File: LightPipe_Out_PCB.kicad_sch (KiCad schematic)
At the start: 9 parts, among them J1 Conn_01x03, J2 Conn_01x02, J3 Conn_01x04, J4 Conn_01x04, J5 Conn_01x04, J6 Conn_01x01, J7 Conn_01x01, J8 Conn_01x02, J9 Conn_01x03

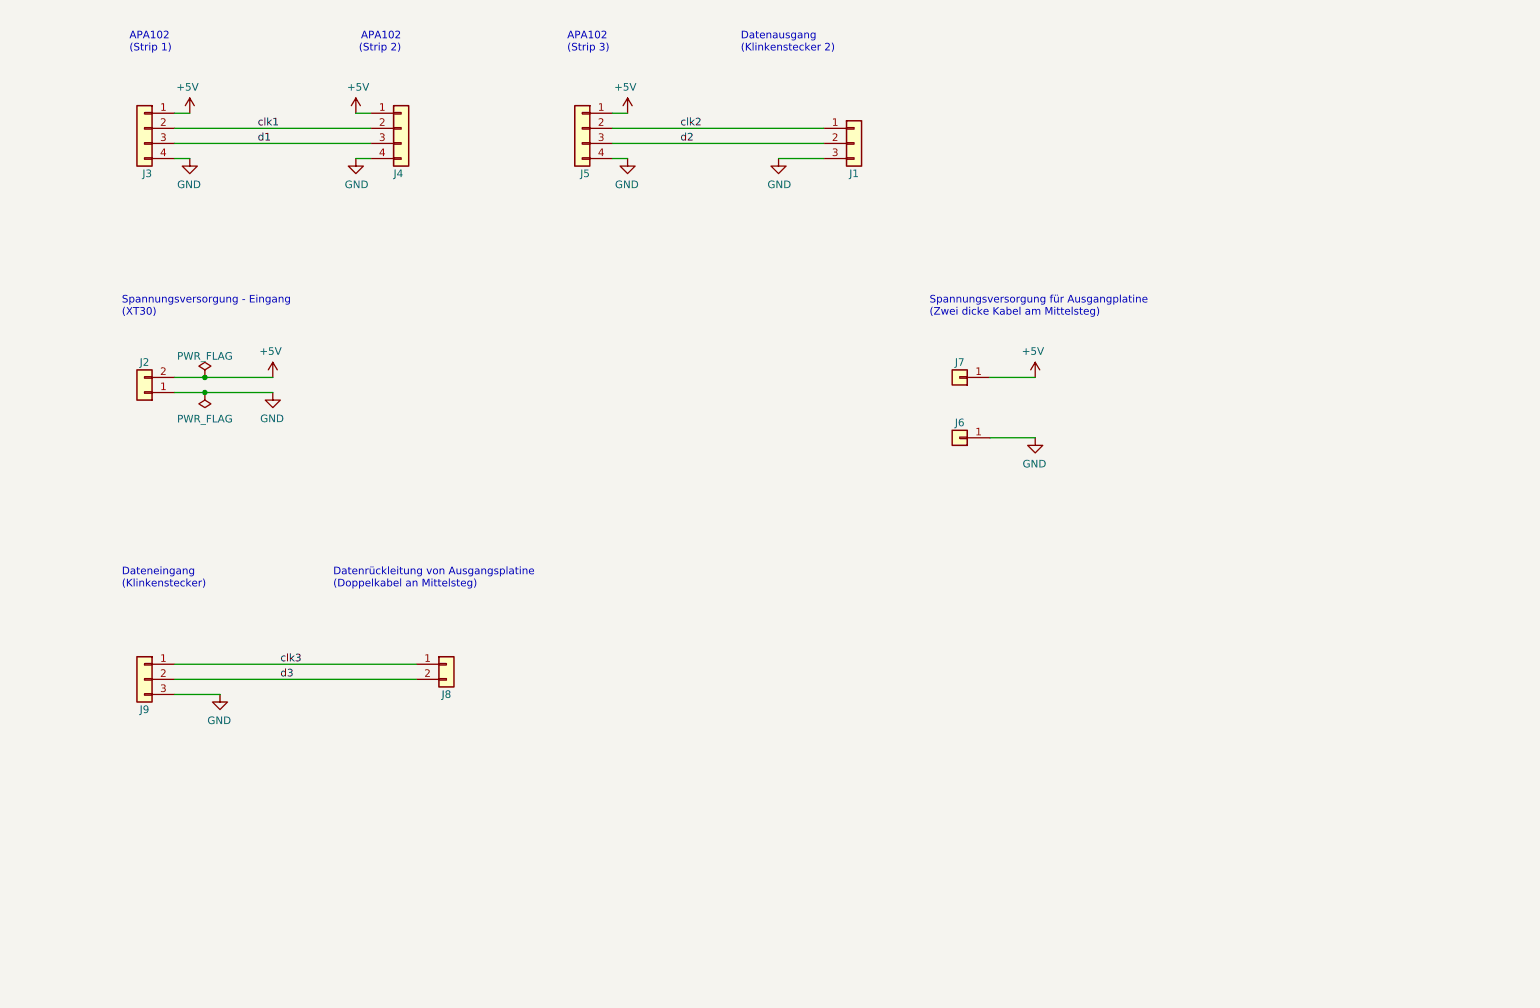
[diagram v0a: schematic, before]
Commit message: [PCB] New Design features to use the PCB as In- and Out-PCB
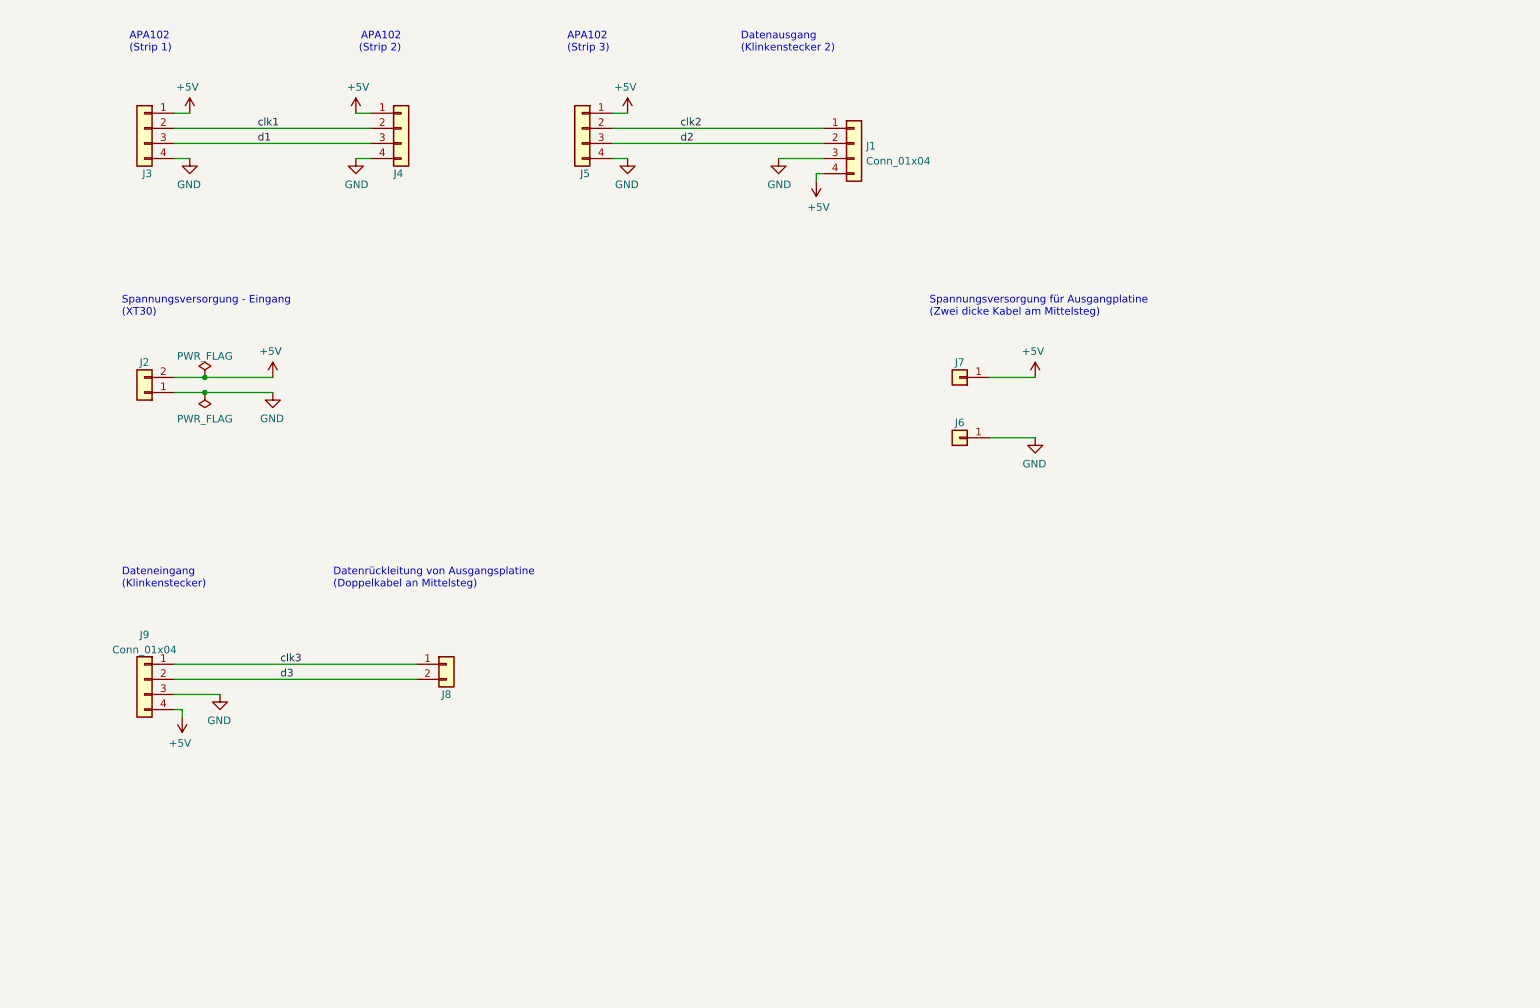
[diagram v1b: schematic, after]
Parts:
- removed J1, J9: Conn_01x03, h8-Connectors:Lumberg-KLB-4-Klinkensteckverbinder-3_5, symbol Connector_Generic:Conn_01x03
- added J1, J9: Conn_01x04, h8-Connectors:Lumberg-KLB-4-Klinkensteckverbinder-3_5-180deg-turnable, symbol Connector_Generic:Conn_01x04
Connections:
- net +5V: now also J1.4 (Pin_4), J9.4 (Pin_4)
- net GND: now also J1.3 (Pin_3), J9.3 (Pin_3)
- net clk2: now also J1.1 (Pin_1)
- net clk3: now also J9.1 (Pin_1)
- net d2: now also J1.2 (Pin_2)
- net d3: now also J9.2 (Pin_2)
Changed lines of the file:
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@@
+    (stroke (width 0) (type default) (color 0 0 0 0))
+  )
+  (wire (pts (xy 48.26 144.78) (xy 48.26 143.51))
     (stroke (width 0) (type default) (color 0 0 0 0))
   )
@@
     (stroke (width 0) (type default) (color 0 0 0 0))
   )
+  (wire (pts (xy 154.94 54.61) (xy 154.94 53.34))
+    (stroke (width 0) (type default) (color 0 0 0 0))
+  )
   (wire (pts (xy 46.99 87.63) (xy 52.07 87.63))
     (stroke (width 0) (type default) (color 0 0 0 0))
@@
     (stroke (width 0) (type default) (color 0 0 0 0))
   )
+  (wire (pts (xy 154.94 53.34) (xy 156.21 53.34))
+    (stroke (width 0) (type default) (color 0 0 0 0))
+  )
   (wire (pts (xy 46.99 48.26) (xy 80.01 48.26))
     (stroke (width 0) (type default) (color 0 0 0 0))
@@
   )
   (wire (pts (xy 80.01 50.8) (xy 77.47 50.8))
+    (stroke (width 0) (type default) (color 0 0 0 0))
+  )
+  (wire (pts (xy 48.26 143.51) (xy 46.99 143.51))
     (stroke (width 0) (type default) (color 0 0 0 0))
   )
@@
     )
     (pin "1")
-  )
-  (symbol (lib_id "Connector_Generic:Conn_01x03") (at 161.29 48.26 0) (unit 1)
-    (in_bom yes) (on_board yes)
-    (property "Reference" "J1" (id 0) (at 161.29 53.34 0))
-    (property "Value" "Conn_01x03" (id 1) (at 159.258 54.2036 0)
-      (effects (font (size 1.27 1.27)) hide)
-    )
-    (property "Footprint" "h8-Connectors:Lumberg-KLB-4-Klinkensteckverbinder-3_5" (id 2) (at 161.29 48.26 0)
-      (effects (font (size 1.27 1.27)) hide)
-    )
-    (property "Datasheet" "~" (id 3) (at 161.29 48.26 0)
-      (effects (font (size 1.27 1.27)) hide)
-    )
-    (pin "1")
-    (pin "2")
-    (pin "3")
-  )
-  (symbol (lib_id "Connector_Generic:Conn_01x03") (at 41.91 138.43 0) (mirror y) (unit 1)
-    (in_bom yes) (on_board yes)
-    (property "Reference" "J9" (id 0) (at 41.91 143.51 0))
-    (property "Value" "Conn_01x03" (id 1) (at 43.942 144.3736 0)
-      (effects (font (size 1.27 1.27)) hide)
-    )
-    (property "Footprint" "h8-Connectors:Lumberg-KLB-4-Klinkensteckverbinder-3_5" (id 2) (at 41.91 138.43 0)
-      (effects (font (size 1.27 1.27)) hide)
-    )
-    (property "Datasheet" "~" (id 3) (at 41.91 138.43 0)
-      (effects (font (size 1.27 1.27)) hide)
-    )
-    (pin "1")
-    (pin "2")
-    (pin "3")
   )
   (symbol (lib_id "Connector_Generic:Conn_01x02") (at 41.91 90.17 180) (unit 1)
@@
     (pin "1")
   )
+  (symbol (lib_id "power:+5V") (at 48.26 144.78 180) (unit 1)
+    (in_bom yes) (on_board yes)
+    (property "Reference" "#PWR0109" (id 0) (at 48.26 140.97 0)
+      (effects (font (size 1.27 1.27)) hide)
+    )
+    (property "Value" "+5V" (id 1) (at 47.879 149.1742 0))
+    (property "Footprint" "" (id 2) (at 48.26 144.78 0)
+      (effects (font (size 1.27 1.27)) hide)
+    )
+    (property "Datasheet" "" (id 3) (at 48.26 144.78 0)
+      (effects (font (size 1.27 1.27)) hide)
+    )
+    (pin "1")
+  )
+  (symbol (lib_id "Connector_Generic:Conn_01x04") (at 161.29 48.26 0) (unit 1)
+    (in_bom yes) (on_board yes) (fields_autoplaced)
+    (property "Reference" "J1" (id 0) (at 163.322 48.6953 0)
+      (effects (font (size 1.27 1.27)) (justify left))
+    )
+    (property "Value" "Conn_01x04" (id 1) (at 163.322 51.2322 0)
+      (effects (font (size 1.27 1.27)) (justify left))
+    )
+    (property "Footprint" "h8-Connectors:Lumberg-KLB-4-Klinkensteckverbinder-3_5-180deg-turnable" (id 2) (at 161.29 48.26 0)
+      (effects (font (size 1.27 1.27)) hide)
+    )
+    (property "Datasheet" "~" (id 3) (at 161.29 48.26 0)
+      (effects (font (size 1.27 1.27)) hide)
+    )
+    (pin "1")
+    (pin "2")
+    (pin "3")
+    (pin "4")
+  )
+  (symbol (lib_id "Connector_Generic:Conn_01x04") (at 41.91 138.43 0) (mirror y) (unit 1)
+    (in_bom yes) (on_board yes) (fields_autoplaced)
+    (property "Reference" "J9" (id 0) (at 41.91 130.9202 0))
+    (property "Value" "Conn_01x04" (id 1) (at 41.91 133.4571 0))
+    (property "Footprint" "h8-Connectors:Lumberg-KLB-4-Klinkensteckverbinder-3_5-180deg-turnable" (id 2) (at 41.91 138.43 0)
+      (effects (font (size 1.27 1.27)) hide)
+    )
+    (property "Datasheet" "~" (id 3) (at 41.91 138.43 0)
+      (effects (font (size 1.27 1.27)) hide)
+    )
+    (pin "1")
+    (pin "2")
+    (pin "3")
+    (pin "4")
+  )
+  (symbol (lib_id "power:+5V") (at 154.94 54.61 0) (mirror x) (unit 1)
+    (in_bom yes) (on_board yes)
+    (property "Reference" "#PWR0110" (id 0) (at 154.94 50.8 0)
+      (effects (font (size 1.27 1.27)) hide)
+    )
+    (property "Value" "+5V" (id 1) (at 155.321 59.0042 0))
+    (property "Footprint" "" (id 2) (at 154.94 54.61 0)
+      (effects (font (size 1.27 1.27)) hide)
+    )
+    (property "Datasheet" "" (id 3) (at 154.94 54.61 0)
+      (effects (font (size 1.27 1.27)) hide)
+    )
+    (pin "1")
+  )
   (symbol (lib_id "power:PWR_FLAG") (at 52.07 87.63 0) (unit 1)
     (in_bom yes) (on_board yes) (fields_autoplaced)
@@
       (reference "#PWR0108") (unit 1) (value "GND") (footprint "")
     )
-    (path "/00000000-0000-0000-0000-00005f9461d7"
-      (reference "J1") (unit 1) (value "Conn_01x03") (footprint "h8-Connectors:Lumberg-KLB-4-Klinkensteckverbinder-3_5")
+    (path "/41571e1e-d333-463a-84fd-29dc2000eb0b"
+      (reference "#PWR0109") (unit 1) (value "+5V") (footprint "")
+    )
+    (path "/7d2c7984-6535-44bc-a86c-9cec98125d73"
+      (reference "#PWR0110") (unit 1) (value "+5V") (footprint "")
+    )
+    (path "/52137419-c203-4dbe-a47e-235ddc4fd115"
+      (reference "J1") (unit 1) (value "Conn_01x04") (footprint "h8-Connectors:Lumberg-KLB-4-Klinkensteckverbinder-3_5-180deg-turnable")
     )
     (path "/00000000-0000-0000-0000-00005f94666b"
@@
       (reference "J8") (unit 1) (value "Conn_01x02") (footprint "Connector_PinHeader_2.00mm:PinHeader_1x02_P2.00mm_Vertical")
     )
-    (path "/00000000-0000-0000-0000-00005f94634e"
-      (reference "J9") (unit 1) (value "Conn_01x03") (footprint "h8-Connectors:Lumberg-KLB-4-Klinkensteckverbinder-3_5")
-    )
-  )
+    (path "/771c4cae-8f80-4832-b07b-977abc522dad"
+      (reference "J9") (unit 1) (value "Conn_01x04") (footprint "h8-Connectors:Lumberg-KLB-4-Klinkensteckverbinder-3_5-180deg-turnable")
+    )
+  )

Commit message: Changed designators from J? to X? and LD? | Improved Footprints
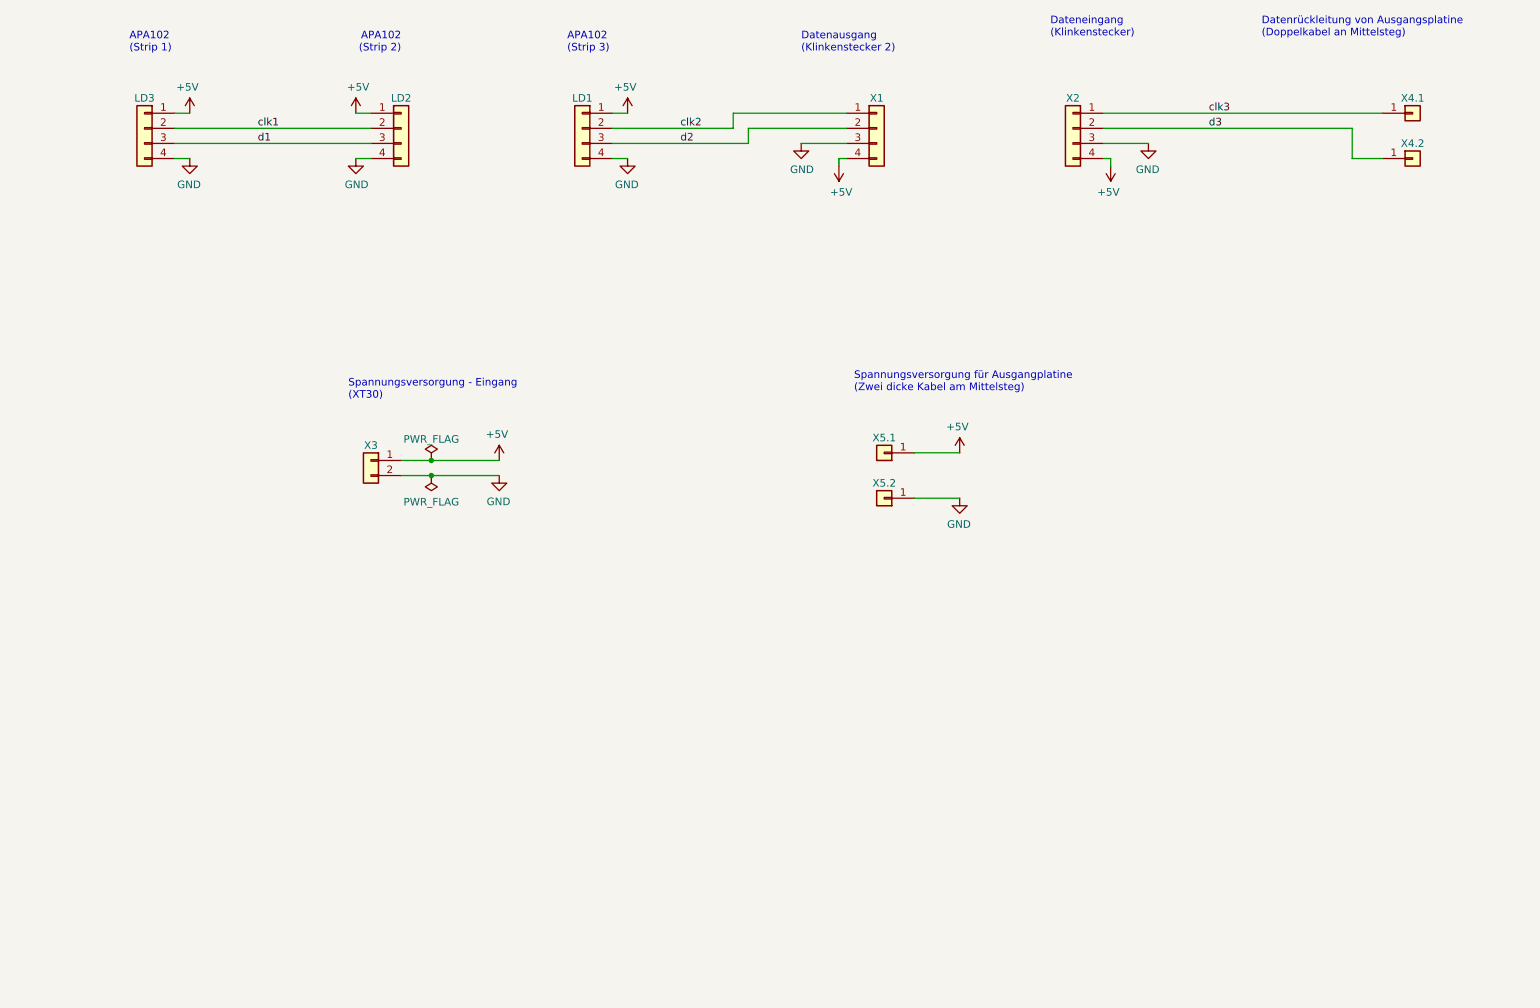
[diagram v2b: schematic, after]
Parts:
- removed J8: Conn_01x02, Connector_PinHeader_2.00mm:PinHeader_1x02_P2.00mm_Vertical, symbol Connector_Generic:Conn_01x02
- added X4.1, X4.2: Conn_01x01, Connector_Wire:SolderWire-0.15sqmm_1x01_D0.5mm_OD1.5mm, symbol Connector_Generic:Conn_01x01
- renumbered J5 to LD1, J4 to LD2, J3 to LD3, J1 to X1, J9 to X2, J2 to X3, J7 to X5.1, J6 to X5.2
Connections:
- net +5V: now also X3.1 (Pin_1); no longer X3.2 (Pin_2)
- net GND: now also X3.2 (Pin_2); no longer X3.1 (Pin_1)
- net clk3: now also X4.1.1 (Pin_1)
- net d3: now also X4.2.1 (Pin_1)
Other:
- moved on the sheet: X1, X2, X3, X5.1, X5.2

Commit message: [PCB] Improved footprints | optimized footprint locations | optimized wires
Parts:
- X4.1, X4.2: footprint Connector_Wire:SolderWire-0.15sqmm_1x01_D0.5mm_OD1.5mm -> h8-Connectors:Solder-Pad-THT-0.7mm
- X5.1, X5.2: footprint Connector_Wire:SolderWire-0.15sqmm_1x01_D0.5mm_OD1.5mm -> h8-Connectors:Solder-Pad-THT-1.5mm
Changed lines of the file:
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@@
       (effects (font (size 1.27 1.27)) hide)
     )
-    (property "Footprint" "Connector_Wire:SolderWire-0.15sqmm_1x01_D0.5mm_OD1.5mm" (id 2) (at 166.37 107.95 0)
+    (property "Footprint" "h8-Connectors:Solder-Pad-THT-1.5mm" (id 2) (at 166.37 107.95 0)
       (effects (font (size 1.27 1.27)) hide)
     )
@@
       (effects (font (size 1.27 1.27)) hide)
     )
-    (property "Footprint" "Connector_Wire:SolderWire-0.15sqmm_1x01_D0.5mm_OD1.5mm" (id 2) (at 166.37 100.33 0)
+    (property "Footprint" "h8-Connectors:Solder-Pad-THT-1.5mm" (id 2) (at 166.37 100.33 0)
       (effects (font (size 1.27 1.27)) hide)
     )
@@
       (effects (font (size 1.27 1.27)) hide)
     )
-    (property "Footprint" "Connector_Wire:SolderWire-0.15sqmm_1x01_D0.5mm_OD1.5mm" (id 2) (at 255.27 50.8 0)
+    (property "Footprint" "h8-Connectors:Solder-Pad-THT-0.7mm" (id 2) (at 255.27 50.8 0)
       (effects (font (size 1.27 1.27)) hide)
     )
@@
       (effects (font (size 1.27 1.27)) hide)
     )
-    (property "Footprint" "Connector_Wire:SolderWire-0.15sqmm_1x01_D0.5mm_OD1.5mm" (id 2) (at 255.27 43.18 0)
+    (property "Footprint" "h8-Connectors:Solder-Pad-THT-0.7mm" (id 2) (at 255.27 43.18 0)
       (effects (font (size 1.27 1.27)) hide)
     )
@@
     )
     (path "/ea7784c2-710b-445a-ba50-3da775d876ed"
-      (reference "X4.1") (unit 1) (value "Conn_01x01") (footprint "Connector_Wire:SolderWire-0.15sqmm_1x01_D0.5mm_OD1.5mm")
+      (reference "X4.1") (unit 1) (value "Conn_01x01") (footprint "h8-Connectors:Solder-Pad-THT-0.7mm")
     )
     (path "/24cb6112-8d07-4162-b71e-d29d9e542042"
-      (reference "X4.2") (unit 1) (value "Conn_01x01") (footprint "Connector_Wire:SolderWire-0.15sqmm_1x01_D0.5mm_OD1.5mm")
+      (reference "X4.2") (unit 1) (value "Conn_01x01") (footprint "h8-Connectors:Solder-Pad-THT-0.7mm")
     )
     (path "/00000000-0000-0000-0000-00005f946830"
-      (reference "X5.1") (unit 1) (value "Conn_01x01") (footprint "Connector_Wire:SolderWire-0.15sqmm_1x01_D0.5mm_OD1.5mm")
+      (reference "X5.1") (unit 1) (value "Conn_01x01") (footprint "h8-Connectors:Solder-Pad-THT-1.5mm")
     )
     (path "/00000000-0000-0000-0000-00005f9467ba"
-      (reference "X5.2") (unit 1) (value "Conn_01x01") (footprint "Connector_Wire:SolderWire-0.15sqmm_1x01_D0.5mm_OD1.5mm")
-    )
-  )
+      (reference "X5.2") (unit 1) (value "Conn_01x01") (footprint "h8-Connectors:Solder-Pad-THT-1.5mm")
+    )
+  )
